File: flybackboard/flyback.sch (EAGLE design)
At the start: 5 parts

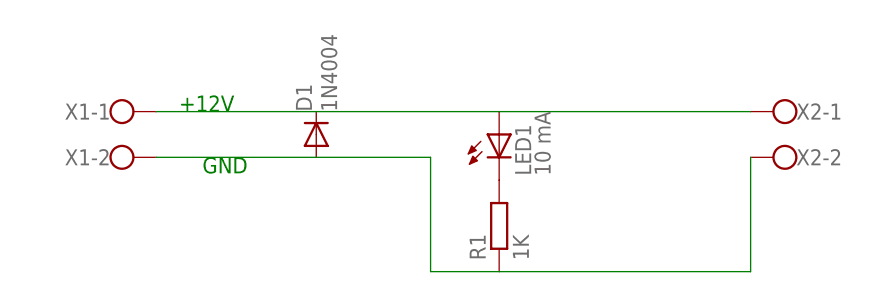
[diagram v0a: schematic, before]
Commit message: update flyback schema
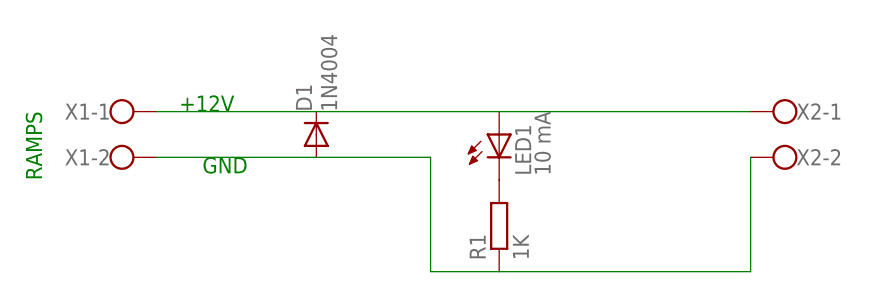
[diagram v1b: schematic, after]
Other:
- note added: "RAMPS"
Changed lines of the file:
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@@
 <text x="0" y="86.36" size="1.778" layer="91">+12V</text>
 <text x="7.62" y="81.28" size="1.778" layer="91" rot="R180">GND</text>
+<text x="-15.24" y="78.74" size="1.778" layer="91" rot="R90">RAMPS</text>
 </plain>
 <instances>
